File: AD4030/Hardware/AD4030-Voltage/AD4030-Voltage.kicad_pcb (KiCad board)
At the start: 4 copper layers, 110 x 70 mm, 186 parts, among them J201 1710072, J401 Conn_01x08, J402 Conn_01x07, J403 PMOD, J404 PMOD, J501 1715721, K201 UMS05-1A80-75D, Q201 MMBT3904, Q501 SI5618A, Q502 MMBT3904, U201 ADG5236BCPZ, U202 LT5400-1, U203 ADA4817-1ACP, U204 ADA4817-1ACP, U205 LT5400-4, U206 LT5400-4, U207 LT5400-4, U208 LT5400-4, U209 LT5400-8, U210 TXB0101DBV, U211 LMH6611, U212 LMH6611, U301 AD8475ACPZ, U302 SN74AUC1G79DBVR, U303 AD4030-24, U304 MAX6350ESA, U401 ADuM260N, U402 ADuM260N, U501 TPS65133DPDR, U502 TSR_1-2433, U503 TEC3-2419WI, U504 LT1763CDE-ADJ, U505 LT1763CDE-1.8, U506 LT1763IDE-3.3, U507 TSR_1-2450, X301 ECS-2520MV-1000-BN-TR

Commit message: PCB layout
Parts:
- moved R303 0.64 mm to (143.5, 110.4)
- moved C301 0.51 mm to (143.5, 108.2)
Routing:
- net /Isolation/CONN_BUSY: track 15.7 -> 23.9 mm
- net GND: track 54.6 -> 60.5 mm, vias 43 -> 67
- net /Isolation/CONN_SDO1: track 15.6 -> 21.6 mm
- net /Isolation/CONN_SDO3: track 16.7 -> 22.7 mm
- net /Isolation/CONN_100MHz: track 17.0 -> 22.9 mm
- net /Isolation/CONN_SDO0: track 14.3 -> 20.2 mm
- net /Isolation/CONN_SDO2: track 16.5 -> 22.4 mm
- net +5VA: track 49.6 -> 47.1 mm
- net /DIFF/GAIN_x20: track 45.1 -> 46.6 mm
- net Net-(U201-Pad10): track 17.4 -> 18.9 mm
- net +5V: track 87.4 -> 88.8 mm
- net -5VA: track 45.0 -> 43.7 mm
- net GNDS: track 2.13 -> 3.37 mm, vias 14 -> 15
- net Net-(R222-Pad2): track 9.26 -> 10.1 mm
- net /ADC/SYNC_CNV: track 11.9 -> 12.7 mm
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- added copper zone on B.Cu, net -5VA
- added copper zone on B.Cu, net Net-(U502-Vout)
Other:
- board text added: "AD4030-24 TEST BOARD"
- board text added: "MODULE FOR ARTY Z7"
- board text removed: "AD4030-24 TEST BOARD MODULE FOR ARTY Z7"

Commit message: PCB layout
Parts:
- added D503: RED, LED_SMD:LED_0603_1608Metric, F.Cu at (128.3, 71.2)
- added R505: 680, Resistor_SMD:R_0603_1608Metric_Pad0.98x0.95mm_HandSolder, F.Cu at (128.3, 74.5)
- added R506: 0, Resistor_SMD:R_0603_1608Metric_Pad0.98x0.95mm_HandSolder, F.Cu at (173.7, 75.9)
- R211, R212: value 91 -> 91/.1%
- R503: value R -> 10k5
- R504: value R -> 10k
- U211, U212: value LMH6611 -> LMH6611MK
- moved K201 4.00 mm to (120.1, 114.9)
- moved C232 0.76 mm to (128.1, 116.8)
- moved C233 0.76 mm to (131.3, 114.0)
- moved Q201 0.76 mm to (124.1, 116.7)
- moved R221 0.76 mm to (124.1, 113.0)
- moved U210 0.76 mm to (128.1, 114.0)
- renumbered U202 to RN202, U205 to RN205, U206 to RN206, U207 to RN207, U208 to RN208, U209 to RN209
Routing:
- net -5VA: track 43.7 -> 53.5 mm
- net Net-(U502-Vout): track 1.57 -> 6.34 mm
- net Net-(U203--): track 33.3 -> 28.9 mm
- net Net-(C227-Pad1): track 14.0 -> 9.70 mm
- net +5V: track 88.8 -> 86.0 mm
- net Net-(Q201-C): track 5.12 -> 7.43 mm
- net VCCQ: track 3.73 -> 5.88 mm
- net GND: track 60.5 -> 62.7 mm, vias 67 -> 89
- net Net-(D503-K): track 0.00 -> 1.60 mm
- net /DIFF/Gain_x10: track 33.9 -> 34.9 mm
- net GNDS: vias 15 -> 31
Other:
- outline, holes or cut-outs redrawn
- board text added: "1"
- board text added: "100MHz"
- board text added: "2"
- board text added: "24V"
- board text added: "3"
- board text added: "4"
- board text added: "AD4030-24 TEST BOARD V1.0"
- board text added: "BUSY"
- board text added: "CNV"
- board text added: "GAIN x10"
- board text added: "GAIN x20"
- board text added: "SCK"
- board text added: "SDI"
- board text added: "SDO0"
- board text added: "SDO1"
- board text added: "SDO2"
- board text added: "SDO3"
- board text added: "~{CS}"
- board text removed: "AD4030-24 TEST BOARD"

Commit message: PCB layout
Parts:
- added C233: 0.1u, Capacitor_SMD:C_0603_1608Metric_Pad1.08x0.95mm_HandSolder, F.Cu at (139.8, 114.0)
- added C235: 0.1u, Capacitor_SMD:C_0603_1608Metric_Pad1.08x0.95mm_HandSolder, F.Cu at (147.3, 114.0)
- added U207: TXB0101DBV, Package_TO_SOT_SMD:SOT-23-6, F.Cu at (143.5, 114.0)
- C315: value 1u -> 10u
- C318, C319: value 2u2 -> 10u
- RN301: value MPMT2002AT5 -> MPMT2003AT5
- U201: value ADG5236BCPZ -> ADG1436YCPZ
- U304: value MAX6350ESA -> LTC6655BHMS8-4.096; footprint Package_SO:SOIC-8_3.9x4.9mm_P1.27mm -> Package_SO:MSOP-8_3x3mm_P0.65mm
- moved C307 0.38 mm to (147.3, 107.4)
- moved C308 0.38 mm to (147.3, 102.7)
- moved R304 0.38 mm to (147.3, 104.5)
- moved R305 0.38 mm to (147.3, 105.5)
- moved R306 0.38 mm to (147.3, 104.5)
- moved C310 0.25 mm to (149.1, 105.0)
- moved L503 0.13 mm to (174.2, 72.6)
- moved U304 0.13 mm to (135.9, 88.9)
- renumbered C233 to C234, RN202 to RN201, RN205 to RN202, RN206 to RN203, RN207 to RN204, RN208 to RN205, RN209 to RN206, U203 to U202, U204 to U203, U210 to U204, U211 to U205, U212 to U206
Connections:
- net +2V5 renamed VCOM
- C314 pad 1: Net-(U304-IN) -> Net-(U304-VIN)
- C318 pad 1: +5VREF -> VDDF
- FB301 pad 2: Net-(U304-IN) -> Net-(U304-VIN)
- R307 pad 1: +5VREF -> VDDF
- R308 pad 1: +5VREF -> VDDF
- RN301 pad 1: +5VREF -> VDDF
- U201 pad 15: /DIFF/GAIN_x20 -> /DIFF/SW_GAIN_x20
- U201 pad 6: /DIFF/GAIN_x20 -> /DIFF/SW_GAIN_x20
- U304 pad 1: unconnected-(U304-NC-Pad1) -> Net-(U304-VIN)
- U304 pad 2: Net-(U304-IN) -> Net-(U304-VIN)
- U304 pad 3: Net-(U304-NR) -> GND
- U304 pad 5: unconnected-(U304-TRIM-Pad5) -> GND
- U304 pad 6: +5VREF -> Net-(U304-NR)
- U304 pad 7: unconnected-(U304-NC-Pad7) -> VDDF
- U304 pad 8: unconnected-(U304-NC-Pad8) -> GND
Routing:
- net /DIFF/SW_GAIN_x20: track 0.00 -> 29.6 mm, vias 0 -> 3
- net /DIFF/GAIN_x20: track 46.6 -> 17.8 mm, vias 3 -> 0
- net VDDF: track 0.00 -> 28.0 mm, vias 0 -> 1
- net +5VREF: track 25.9 -> 0.00 mm, vias 1 -> 0
- net +5V: track 86.0 -> 107.3 mm, vias 7 -> 8
- net GND: track 62.7 -> 54.7 mm, vias 89 -> 141
- net +1V8: track 20.6 -> 27.6 mm, vias 13 -> 14
- net Net-(U304-VIN): track 0.00 -> 5.90 mm
- net Net-(U304-IN): track 4.45 -> 0.00 mm
- net GNDS: track 3.37 -> 0.00 mm, vias 31 -> 38
- net Net-(U304-NR): track 2.31 -> 4.69 mm
- net /DIFF/Gain_x10: track 34.9 -> 36.9 mm
- net Net-(R308-Pad2): track 14.0 -> 15.8 mm
- net Net-(U202-FB): track 15.7 -> 17.5 mm
- net Net-(R222-Pad1): track 20.7 -> 22.0 mm
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- added copper zone on B.Cu, net Net-(U501-VPOS)
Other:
- outline, holes or cut-outs redrawn

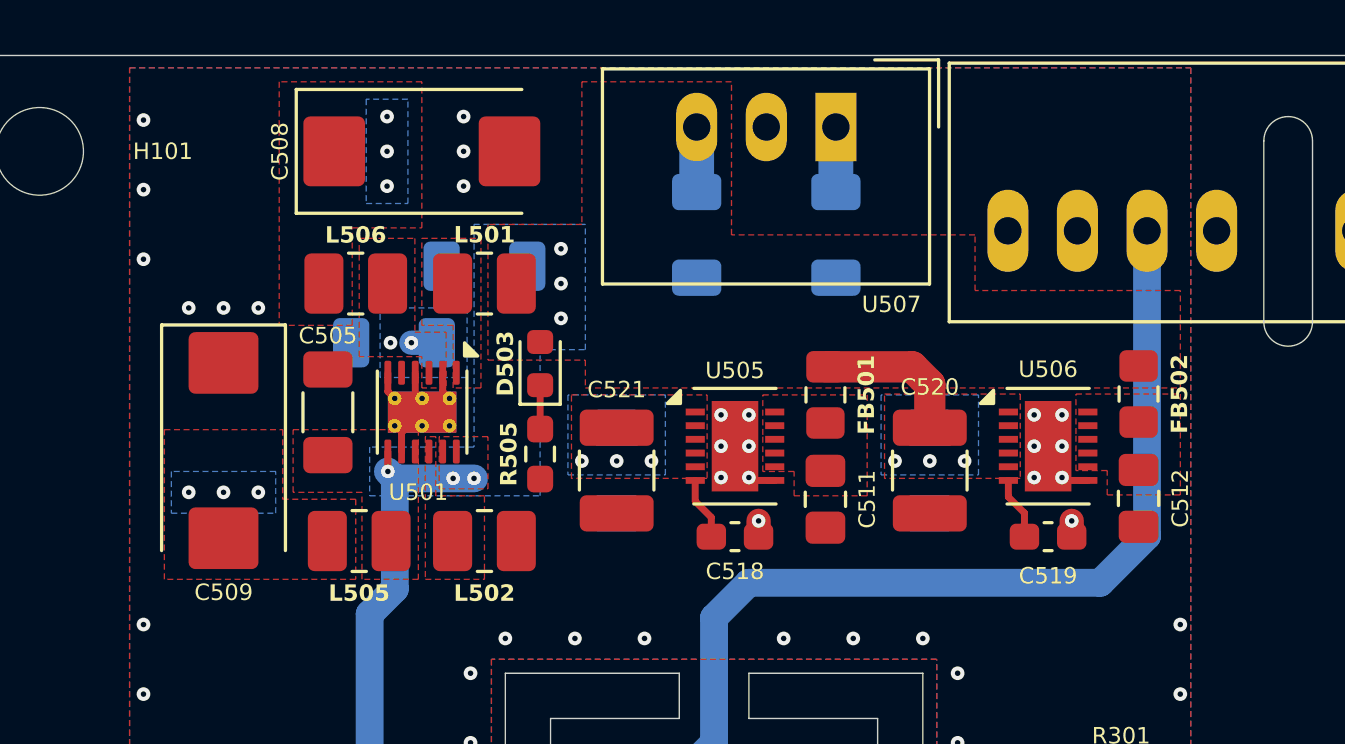
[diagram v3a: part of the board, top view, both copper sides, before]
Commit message: Bug fixes in PCB.
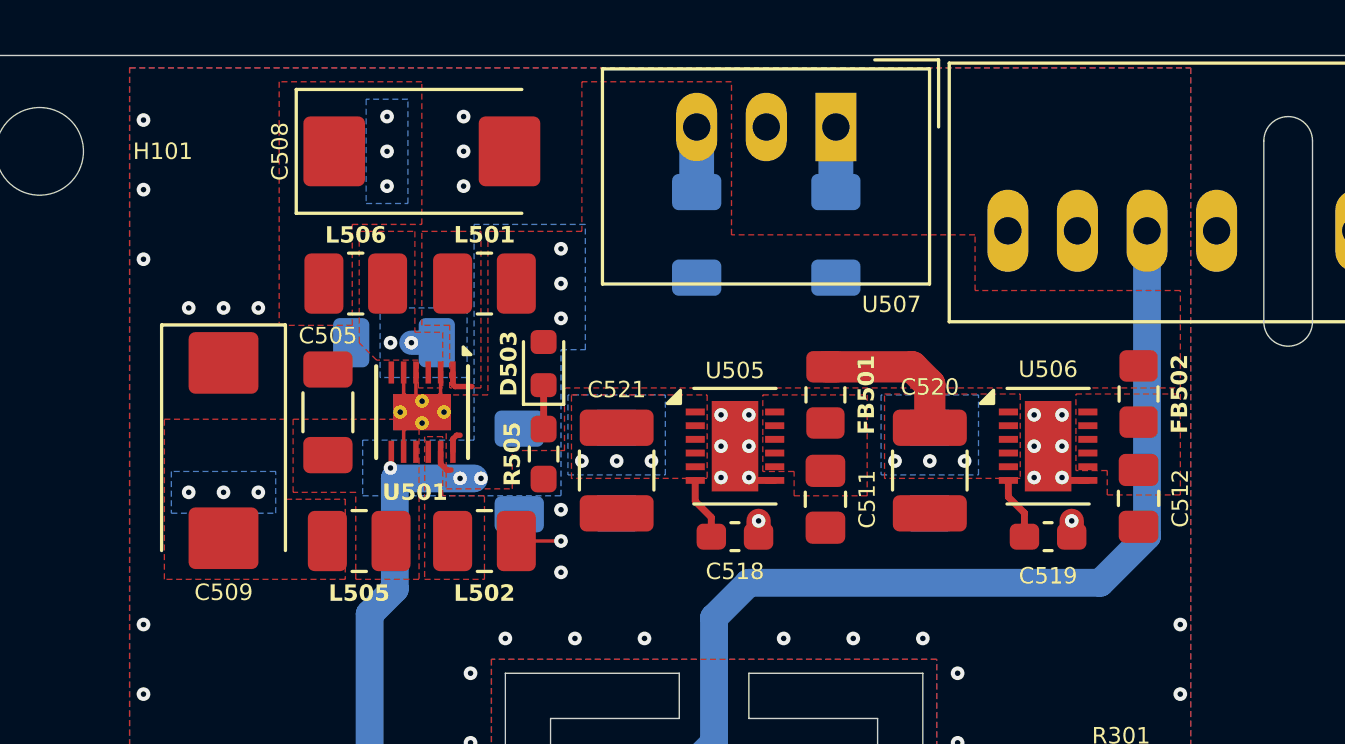
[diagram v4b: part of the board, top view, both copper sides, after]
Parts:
- U501: footprint Package_SON:WSON-12-1EP_3x3mm_P0.5mm_EP1.5x2.5mm_ThermalVias -> AD4030:DPD12_TEX
- moved C501 7.60 mm to (127.5, 75.2), turned to -90 degrees
- moved D503 0.13 mm to (128.4, 71.2)
- moved R505 0.13 mm to (128.4, 74.5)
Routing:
- net GND: track 54.7 -> 57.6 mm, vias 141 -> 144
- net +5V: track 107.3 -> 108.5 mm
- net Net-(U501-SWP): track 0.00 -> 1.16 mm
